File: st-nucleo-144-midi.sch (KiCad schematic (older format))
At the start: 4 parts, among them J1 Conn_02x08_Odd_Even, J2 Conn_02x15_Odd_Even, J3 Conn_02x10_Odd_Even, J4 Conn_02x17_Odd_Even

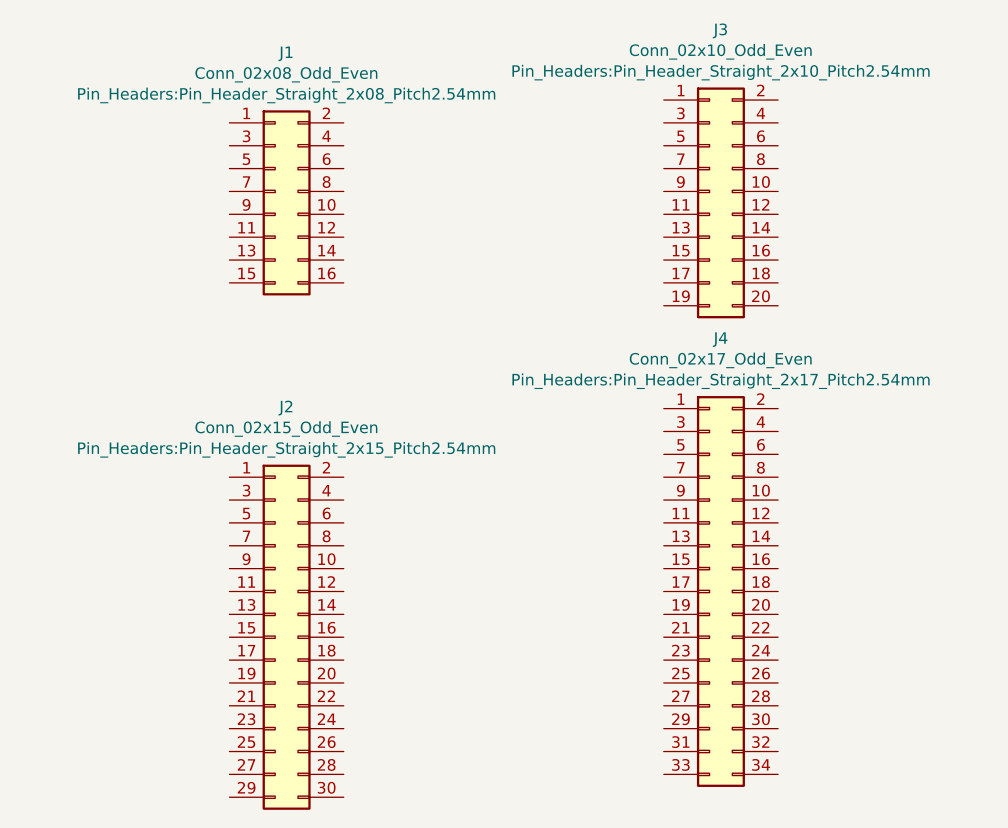
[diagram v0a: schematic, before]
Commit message: Add labels to J1, J2. Update Gerber plot parameters.
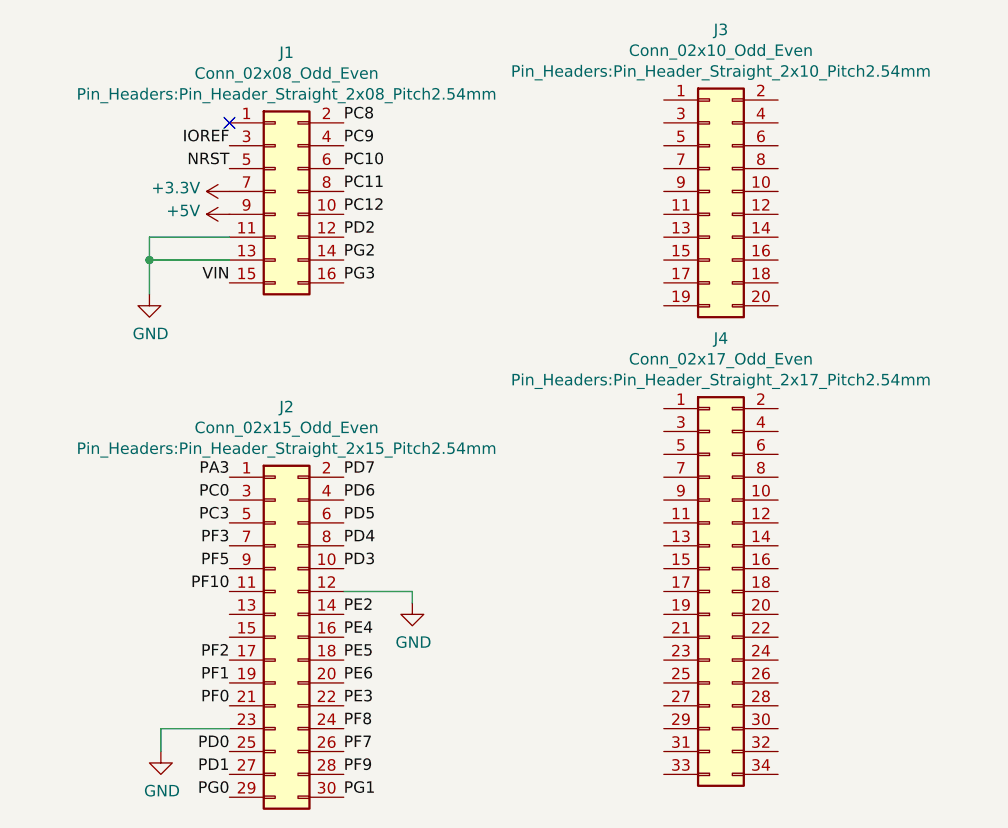
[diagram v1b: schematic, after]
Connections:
- net PC12: now reaches J1.10 (Pin_10)
- net GND: now reaches J1.11 (Pin_11)
- net GND: now also J1.13 (Pin_13), J2.12 (Pin_12), J2.23 (Pin_23)
- net PD2: now reaches J1.12 (Pin_12)
- net PG2: now reaches J1.14 (Pin_14)
- net VIN: now reaches J1.15 (Pin_15)
- net PG3: now reaches J1.16 (Pin_16)
- net PC8: now reaches J1.2 (Pin_2)
- net IOREF: now reaches J1.3 (Pin_3)
- net PC9: now reaches J1.4 (Pin_4)
- net NRST: now reaches J1.5 (Pin_5)
- net PC10: now reaches J1.6 (Pin_6)
- net +3V3: now reaches J1.7 (Pin_7)
- net PC11: now reaches J1.8 (Pin_8)
- net +5V: now reaches J1.9 (Pin_9)
- net PA3: now reaches J2.1 (Pin_1)
- net PD3: now reaches J2.10 (Pin_10)
- net PF10: now reaches J2.11 (Pin_11)
- net PE2: now reaches J2.14 (Pin_14)
- net PE4: now reaches J2.16 (Pin_16)
- net PF2: now reaches J2.17 (Pin_17)
- net PE5: now reaches J2.18 (Pin_18)
- net PF1: now reaches J2.19 (Pin_19)
- net PD7: now reaches J2.2 (Pin_2)
- net PE6: now reaches J2.20 (Pin_20)
- net PF0: now reaches J2.21 (Pin_21)
- net PE3: now reaches J2.22 (Pin_22)
- net PF8: now reaches J2.24 (Pin_24)
- net PD0: now reaches J2.25 (Pin_25)
- net PF7: now reaches J2.26 (Pin_26)
- net PD1: now reaches J2.27 (Pin_27)
- net PF9: now reaches J2.28 (Pin_28)
- net PG0: now reaches J2.29 (Pin_29)
- net PC0: now reaches J2.3 (Pin_3)
- net PG1: now reaches J2.30 (Pin_30)
- net PD6: now reaches J2.4 (Pin_4)
- net PC3: now reaches J2.5 (Pin_5)
- net PD5: now reaches J2.6 (Pin_6)
- net PF3: now reaches J2.7 (Pin_7)
- net PD4: now reaches J2.8 (Pin_8)
- net PF5: now reaches J2.9 (Pin_9)
- no-connect marks 0 -> 1
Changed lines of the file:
@@
 EESchema Schematic File Version 4
+LIBS:st-nucleo-144-midi-cache
 EELAYER 26 0
 EELAYER END
@@
 	1    0    0    -1
 $EndComp
+Text Label 4000 3000 2    50   ~ 0
+IOREF
+Text Label 4000 3100 2    50   ~ 0
+NRST
+$Comp
+L power:+3.3V #PWR?
+U 1 1 5C5BD601
+P 4000 3200
+F 0 "#PWR?" H 4000 3050 50  0001 C CNN
+F 1 "+3.3V" V 4015 3328 50  0000 L CNN
+F 2 "" H 4000 3200 50  0001 C CNN
+F 3 "" H 4000 3200 50  0001 C CNN
+	1    4000 3200
+	0    -1   -1   0
+$EndComp
+$Comp
+L power:+5V #PWR?
+U 1 1 5C5BD656
+P 4000 3300
+F 0 "#PWR?" H 4000 3150 50  0001 C CNN
+F 1 "+5V" V 4015 3428 50  0000 L CNN
+F 2 "" H 4000 3300 50  0001 C CNN
+F 3 "" H 4000 3300 50  0001 C CNN
+	1    4000 3300
+	0    -1   -1   0
+$EndComp
+Text Label 4000 3600 2    50   ~ 0
+VIN
+Text Label 4500 2900 0    50   ~ 0
+PC8
+Text Label 4500 3000 0    50   ~ 0
+PC9
+Text Label 4500 3100 0    50   ~ 0
+PC10
+Text Label 4500 3200 0    50   ~ 0
+PC11
+Text Label 4500 3300 0    50   ~ 0
+PC12
+Text Label 4500 3400 0    50   ~ 0
+PD2
+Text Label 4500 3500 0    50   ~ 0
+PG2
+Text Label 4500 3600 0    50   ~ 0
+PG3
+$Comp
+L power:GND #PWR?
+U 1 1 5C5BD87F
+P 3650 3650
+F 0 "#PWR?" H 3650 3400 50  0001 C CNN
+F 1 "GND" H 3655 3477 50  0000 C CNN
+F 2 "" H 3650 3650 50  0001 C CNN
+F 3 "" H 3650 3650 50  0001 C CNN
+	1    3650 3650
+	1    0    0    -1
+$EndComp
+Wire Wire Line
+	3650 3400 3650 3500
+Connection ~ 3650 3500
+Wire Wire Line
+	3650 3500 3650 3650
+Wire Wire Line
+	3650 3500 4000 3500
+Wire Wire Line
+	3650 3400 4000 3400
+NoConn ~ 4000 2900
+Text Label 4500 4450 0    50   ~ 0
+PD7
+Text Label 4500 4550 0    50   ~ 0
+PD6
+Text Label 4500 4750 0    50   ~ 0
+PD4
+Text Label 4500 4650 0    50   ~ 0
+PD5
+Text Label 4500 4850 0    50   ~ 0
+PD3
+$Comp
+L power:GND #PWR?
+U 1 1 5C5BDA01
+P 4800 5000
+F 0 "#PWR?" H 4800 4750 50  0001 C CNN
+F 1 "GND" H 4805 4827 50  0000 C CNN
+F 2 "" H 4800 5000 50  0001 C CNN
+F 3 "" H 4800 5000 50  0001 C CNN
+	1    4800 5000
+	1    0    0    -1
+$EndComp
+Wire Wire Line
+	4500 4950 4800 4950
+Wire Wire Line
+	4800 4950 4800 5000
+Text Label 4500 5050 0    50   ~ 0
+PE2
+Text Label 4500 5150 0    50   ~ 0
+PE4
+Text Label 4500 5250 0    50   ~ 0
+PE5
+Text Label 4500 5350 0    50   ~ 0
+PE6
+Text Label 4500 5450 0    50   ~ 0
+PE3
+Text Label 4500 5550 0    50   ~ 0
+PF8
+Text Label 4500 5650 0    50   ~ 0
+PF7
+Text Label 4500 5750 0    50   ~ 0
+PF9
+Text Label 4500 5850 0    50   ~ 0
+PG1
+$Comp
+L power:GND #PWR?
+U 1 1 5C5BDB62
+P 3700 5650
+F 0 "#PWR?" H 3700 5400 50  0001 C CNN
+F 1 "GND" H 3705 5477 50  0000 C CNN
+F 2 "" H 3700 5650 50  0001 C CNN
+F 3 "" H 3700 5650 50  0001 C CNN
+	1    3700 5650
+	1    0    0    -1
+$EndComp
+Wire Wire Line
+	4000 5550 3700 5550
+Wire Wire Line
+	3700 5550 3700 5650
+Text Label 4000 4450 2    50   ~ 0
+PA3
+Text Label 4000 4550 2    50   ~ 0
+PC0
+Text Label 4000 4650 2    50   ~ 0
+PC3
+Text Label 4000 4750 2    50   ~ 0
+PF3
+Text Label 4000 4850 2    50   ~ 0
+PF5
+Text Label 4000 4950 2    50   ~ 0
+PF10
+Text Label 4000 5250 2    50   ~ 0
+PF2
+Text Label 4000 5350 2    50   ~ 0
+PF1
+Text Label 4000 5450 2    50   ~ 0
+PF0
+Text Label 4000 5650 2    50   ~ 0
+PD0
+Text Label 4000 5750 2    50   ~ 0
+PD1
+Text Label 4000 5850 2    50   ~ 0
+PG0
 $EndSCHEMATC

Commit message: Added pin labels to J3, J4.
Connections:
- net GND: now also J3.8 (Pin_8), J4.17 (Pin_17), J4.22 (Pin_22), J4.27 (Pin_27), J4.5 (Pin_5)
- net PC6: now reaches J3.1 (Pin_1)
- net PA5: now reaches J3.10 (Pin_10)
- net PC7: now reaches J3.11 (Pin_11)
- net PA6: now reaches J3.12 (Pin_12)
- net PB5: now reaches J3.13 (Pin_13)
- net PA7: now reaches J3.14 (Pin_14)
- net PB3: now reaches J3.15 (Pin_15)
- net PD14: now reaches J3.16 (Pin_16)
- net PA4: now reaches J3.17 (Pin_17)
- net PD15: now reaches J3.18 (Pin_18)
- net PB4: now reaches J3.19 (Pin_19)
- net PB8: now reaches J3.2 (Pin_2)
- net PF12: now reaches J3.20 (Pin_20)
- net PB15: now reaches J3.3 (Pin_3)
- net PB9: now reaches J3.4 (Pin_4)
- net PB13: now reaches J3.5 (Pin_5)
- net AREF: now reaches J3.6 (Pin_6)
- net PB12: now reaches J3.7 (Pin_7)
- net PA15: now reaches J3.9 (Pin_9)
- net VDDA: now reaches J4.1 (Pin_1)
- net PE13: now reaches J4.10 (Pin_10)
- net PF4: now reaches J4.11 (Pin_11)
- net PF15: now reaches J4.12 (Pin_12)
- net PB6: now reaches J4.13 (Pin_13)
- net PG14: now reaches J4.14 (Pin_14)
- net PB2: now reaches J4.15 (Pin_15)
- net PG9: now reaches J4.16 (Pin_16)
- net PE8: now reaches J4.18 (Pin_18)
- net PD13: now reaches J4.19 (Pin_19)
- net PF13: now reaches J4.2 (Pin_2)
- net PE7: now reaches J4.20 (Pin_20)
- net PD12: now reaches J4.21 (Pin_21)
- net PD11: now reaches J4.23 (Pin_23)
- net PE10: now reaches J4.24 (Pin_24)
- net PE2_NC: now reaches J4.25 (Pin_25)
- net PE12: now reaches J4.26 (Pin_26)
- net PE14: now reaches J4.28 (Pin_28)
- net PE14: now also J4.8 (Pin_8)
- net PA0: now reaches J4.29 (Pin_29)
- net GNDA: now reaches J4.3 (Pin_3)
- net PE15: now reaches J4.30 (Pin_30)
- net PB0: now reaches J4.31 (Pin_31)
- net PB10: now reaches J4.32 (Pin_32)
- net PE0: now reaches J4.33 (Pin_33)
- net PB11: now reaches J4.34 (Pin_34)
- net PE9: now reaches J4.4 (Pin_4)
- net PE11: now reaches J4.6 (Pin_6)
- net PB1: now reaches J4.7 (Pin_7)
- net PC2: now reaches J4.9 (Pin_9)
- no-connect marks 1 -> 3
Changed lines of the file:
@@
 Text Label 4000 5850 2    50   ~ 0
 PG0
+NoConn ~ 4000 5050
+NoConn ~ 4000 5150
+Text Label 5900 2800 2    50   ~ 0
+PC6
+Text Label 5900 2900 2    50   ~ 0
+PB15
+Text Label 5900 3000 2    50   ~ 0
+PB13
+Text Label 5900 3100 2    50   ~ 0
+PB12
+Text Label 5900 3200 2    50   ~ 0
+PA15
+Text Label 5900 3300 2    50   ~ 0
+PC7
+Text Label 5900 3400 2    50   ~ 0
+PB5
+Text Label 5900 3500 2    50   ~ 0
+PB3
+Text Label 5900 3600 2    50   ~ 0
+PA4
+Text Label 5900 3700 2    50   ~ 0
+PB4
+Text Label 6400 2800 0    50   ~ 0
+PB8
+Text Label 6400 2900 0    50   ~ 0
+PB9
+Text Label 6400 3000 0    50   ~ 0
+AREF
+$Comp
+L power:GND #PWR?
+U 1 1 5C5E5880
+P 6750 3200
+F 0 "#PWR?" H 6750 2950 50  0001 C CNN
+F 1 "GND" H 6755 3027 50  0000 C CNN
+F 2 "" H 6750 3200 50  0001 C CNN
+F 3 "" H 6750 3200 50  0001 C CNN
+	1    6750 3200
+	1    0    0    -1
+$EndComp
+Wire Wire Line
+	6400 3100 6750 3100
+Wire Wire Line
+	6750 3100 6750 3200
+Text Label 6400 3200 0    50   ~ 0
+PA5
+Text Label 6400 3300 0    50   ~ 0
+PA6
+Text Label 6400 3400 0    50   ~ 0
+PA7
+Text Label 6400 3500 0    50   ~ 0
+PD14
+Text Label 6400 3600 0    50   ~ 0
+PD15
+Text Label 6400 3700 0    50   ~ 0
+PF12
+$Comp
+L power:GND #PWR?
+U 1 1 5C5E59E0
+P 5500 4450
+F 0 "#PWR?" H 5500 4200 50  0001 C CNN
+F 1 "GND" H 5505 4277 50  0000 C CNN
+F 2 "" H 5500 4450 50  0001 C CNN
+F 3 "" H 5500 4450 50  0001 C CNN
+	1    5500 4450
+	1    0    0    -1
+$EndComp
+Wire Wire Line
+	5500 4450 5500 4350
+Wire Wire Line
+	5500 4350 5900 4350
+Text Label 5900 4450 2    50   ~ 0
+PB1
+Text Label 5900 4550 2    50   ~ 0
+PC2
+Text Label 5900 4650 2    50   ~ 0
+PF4
+Text Label 5900 4750 2    50   ~ 0
+PB6
+Text Label 5900 4850 2    50   ~ 0
+PB2
+$Comp
+L power:GND #PWR?
+U 1 1 5C5E5B89
+P 5500 5050
+F 0 "#PWR?" H 5500 4800 50  0001 C CNN
+F 1 "GND" H 5505 4877 50  0000 C CNN
+F 2 "" H 5500 5050 50  0001 C CNN
+F 3 "" H 5500 5050 50  0001 C CNN
+	1    5500 5050
+	1    0    0    -1
+$EndComp
+Wire Wire Line
+	5500 5050 5500 4950
+Wire Wire Line
+	5900 4950 5500 4950
+Text Label 5900 5050 2    50   ~ 0
+PD13
+Text Label 5900 5150 2    50   ~ 0
+PD12
+Text Label 5900 5250 2    50   ~ 0
+PD11
+Text Label 5900 5350 2    50   ~ 0
+PE2_NC
+$Comp
+L power:GND #PWR?
+U 1 1 5C5E5D61
+P 5500 5550
+F 0 "#PWR?" H 5500 5300 50  0001 C CNN
+F 1 "GND" H 5505 5377 50  0000 C CNN
+F 2 "" H 5500 5550 50  0001 C CNN
+F 3 "" H 5500 5550 50  0001 C CNN
+	1    5500 5550
+	1    0    0    -1
+$EndComp
+Wire Wire Line
+	5500 5550 5500 5450
+Wire Wire Line
+	5900 5450 5500 5450
+Text Label 5900 5550 2    50   ~ 0
+PA0
+Text Label 5900 5650 2    50   ~ 0
+PB0
+Text Label 5900 5750 2    50   ~ 0
+PE0
+Text Label 6400 4150 0    50   ~ 0
+PF13
+Text Label 6400 4250 0    50   ~ 0
+PE9
+Text Label 6400 4350 0    50   ~ 0
+PE11
+Text Label 6400 4450 0    50   ~ 0
+PE14
+Text Label 6400 4550 0    50   ~ 0
+PE13
+Text Label 6400 4650 0    50   ~ 0
+PF15
+Text Label 6400 4750 0    50   ~ 0
+PG14
+Text Label 6400 4850 0    50   ~ 0
+PG9
+Text Label 6400 4950 0    50   ~ 0
+PE8
+Text Label 6400 5050 0    50   ~ 0
+PE7
+$Comp
+L power:GND #PWR?
+U 1 1 5C5E5EBA
+P 6850 5250
+F 0 "#PWR?" H 6850 5000 50  0001 C CNN
+F 1 "GND" H 6855 5077 50  0000 C CNN
+F 2 "" H 6850 5250 50  0001 C CNN
+F 3 "" H 6850 5250 50  0001 C CNN
+	1    6850 5250
+	1    0    0    -1
+$EndComp
+Wire Wire Line
+	6400 5150 6850 5150
+Wire Wire Line
+	6850 5150 6850 5250
+Text Label 6400 5250 0    50   ~ 0
+PE10
+Text Label 6400 5350 0    50   ~ 0
+PE12
+Text Label 6400 5450 0    50   ~ 0
+PE14
+Text Label 6400 5550 0    50   ~ 0
+PE15
+Text Label 6400 5650 0    50   ~ 0
+PB10
+Text Label 6400 5750 0    50   ~ 0
+PB11
+$Comp
+L power:GNDA #PWR?
+U 1 1 5C609688
+P 5300 4450
+F 0 "#PWR?" H 5300 4200 50  0001 C CNN
+F 1 "GNDA" H 5305 4277 50  0000 C CNN
+F 2 "" H 5300 4450 50  0001 C CNN
+F 3 "" H 5300 4450 50  0001 C CNN
+	1    5300 4450
+	1    0    0    -1
+$EndComp
+Wire Wire Line
+	5900 4250 5300 4250
+Wire Wire Line
+	5300 4250 5300 4450
+$Comp
+L power:VDDA #PWR?
+U 1 1 5C6098CC
+P 5600 4150
+F 0 "#PWR?" H 5600 4000 50  0001 C CNN
+F 1 "VDDA" V 5618 4278 50  0000 L CNN
+F 2 "" H 5600 4150 50  0001 C CNN
+F 3 "" H 5600 4150 50  0001 C CNN
+	1    5600 4150
+	0    -1   -1   0
+$EndComp
+Wire Wire Line
+	5900 4150 5600 4150
 $EndSCHEMATC

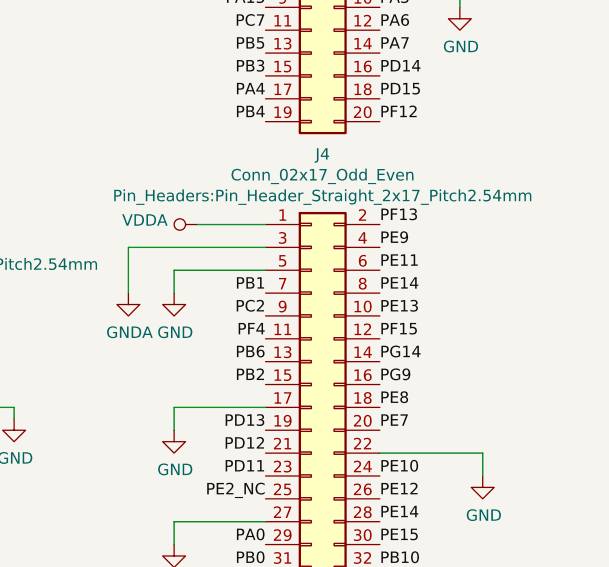
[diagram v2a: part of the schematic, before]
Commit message: Fix misnamed pin
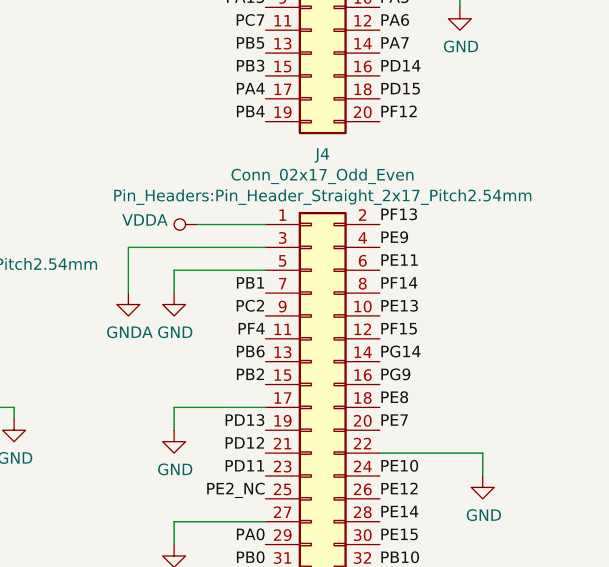
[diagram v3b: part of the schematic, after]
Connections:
- net PE14: no longer J4.8 (Pin_8)
- new net PF14: J4.8 (Pin_8)
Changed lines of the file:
@@
 NRST
 $Comp
-L power:+3.3V #PWR?
+L power:+3.3V #PWR0101
 U 1 1 5C5BD601
 P 4000 3200
-F 0 "#PWR?" H 4000 3050 50  0001 C CNN
+F 0 "#PWR0101" H 4000 3050 50  0001 C CNN
 F 1 "+3.3V" V 4015 3328 50  0000 L CNN
 F 2 "" H 4000 3200 50  0001 C CNN
@@
 $EndComp
 $Comp
-L power:+5V #PWR?
+L power:+5V #PWR0102
 U 1 1 5C5BD656
 P 4000 3300
-F 0 "#PWR?" H 4000 3150 50  0001 C CNN
+F 0 "#PWR0102" H 4000 3150 50  0001 C CNN
 F 1 "+5V" V 4015 3428 50  0000 L CNN
 F 2 "" H 4000 3300 50  0001 C CNN
@@
 PG3
 $Comp
-L power:GND #PWR?
+L power:GND #PWR0103
 U 1 1 5C5BD87F
 P 3650 3650
-F 0 "#PWR?" H 3650 3400 50  0001 C CNN
+F 0 "#PWR0103" H 3650 3400 50  0001 C CNN
 F 1 "GND" H 3655 3477 50  0000 C CNN
 F 2 "" H 3650 3650 50  0001 C CNN
@@
 PD3
 $Comp
-L power:GND #PWR?
+L power:GND #PWR0104
 U 1 1 5C5BDA01
 P 4800 5000
-F 0 "#PWR?" H 4800 4750 50  0001 C CNN
+F 0 "#PWR0104" H 4800 4750 50  0001 C CNN
 F 1 "GND" H 4805 4827 50  0000 C CNN
 F 2 "" H 4800 5000 50  0001 C CNN
@@
 PG1
 $Comp
-L power:GND #PWR?
+L power:GND #PWR0105
 U 1 1 5C5BDB62
 P 3700 5650
-F 0 "#PWR?" H 3700 5400 50  0001 C CNN
+F 0 "#PWR0105" H 3700 5400 50  0001 C CNN
 F 1 "GND" H 3705 5477 50  0000 C CNN
 F 2 "" H 3700 5650 50  0001 C CNN
@@
 AREF
 $Comp
-L power:GND #PWR?
+L power:GND #PWR0106
 U 1 1 5C5E5880
 P 6750 3200
-F 0 "#PWR?" H 6750 2950 50  0001 C CNN
+F 0 "#PWR0106" H 6750 2950 50  0001 C CNN
 F 1 "GND" H 6755 3027 50  0000 C CNN
 F 2 "" H 6750 3200 50  0001 C CNN
@@
 PF12
 $Comp
-L power:GND #PWR?
+L power:GND #PWR0107
 U 1 1 5C5E59E0
 P 5500 4450
-F 0 "#PWR?" H 5500 4200 50  0001 C CNN
+F 0 "#PWR0107" H 5500 4200 50  0001 C CNN
 F 1 "GND" H 5505 4277 50  0000 C CNN
 F 2 "" H 5500 4450 50  0001 C CNN
@@
 PB2
 $Comp
-L power:GND #PWR?
+L power:GND #PWR0108
 U 1 1 5C5E5B89
 P 5500 5050
-F 0 "#PWR?" H 5500 4800 50  0001 C CNN
+F 0 "#PWR0108" H 5500 4800 50  0001 C CNN
 F 1 "GND" H 5505 4877 50  0000 C CNN
 F 2 "" H 5500 5050 50  0001 C CNN
@@
 PE2_NC
 $Comp
-L power:GND #PWR?
+L power:GND #PWR0109
 U 1 1 5C5E5D61
 P 5500 5550
-F 0 "#PWR?" H 5500 5300 50  0001 C CNN
+F 0 "#PWR0109" H 5500 5300 50  0001 C CNN
 F 1 "GND" H 5505 5377 50  0000 C CNN
 F 2 "" H 5500 5550 50  0001 C CNN
@@
 PE11
 Text Label 6400 4450 0    50   ~ 0
-PE14
+PF14
 Text Label 6400 4550 0    50   ~ 0
 PE13
@@
 PE7
 $Comp
-L power:GND #PWR?
+L power:GND #PWR0110
 U 1 1 5C5E5EBA
 P 6850 5250
-F 0 "#PWR?" H 6850 5000 50  0001 C CNN
+F 0 "#PWR0110" H 6850 5000 50  0001 C CNN
 F 1 "GND" H 6855 5077 50  0000 C CNN
 F 2 "" H 6850 5250 50  0001 C CNN
@@
 PB11
 $Comp
-L power:GNDA #PWR?
+L power:GNDA #PWR0111
 U 1 1 5C609688
 P 5300 4450
-F 0 "#PWR?" H 5300 4200 50  0001 C CNN
+F 0 "#PWR0111" H 5300 4200 50  0001 C CNN
 F 1 "GNDA" H 5305 4277 50  0000 C CNN
 F 2 "" H 5300 4450 50  0001 C CNN
@@
 	5300 4250 5300 4450
 $Comp
-L power:VDDA #PWR?
+L power:VDDA #PWR0112
 U 1 1 5C6098CC
 P 5600 4150
-F 0 "#PWR?" H 5600 4000 50  0001 C CNN
+F 0 "#PWR0112" H 5600 4000 50  0001 C CNN
 F 1 "VDDA" V 5618 4278 50  0000 L CNN
 F 2 "" H 5600 4150 50  0001 C CNN
